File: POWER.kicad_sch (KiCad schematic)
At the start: 18 parts, among them IC1 ECP5-BGA256, U1 TPS74633, U2 TPS74618, U3 TPS74625, U4 TPS74611

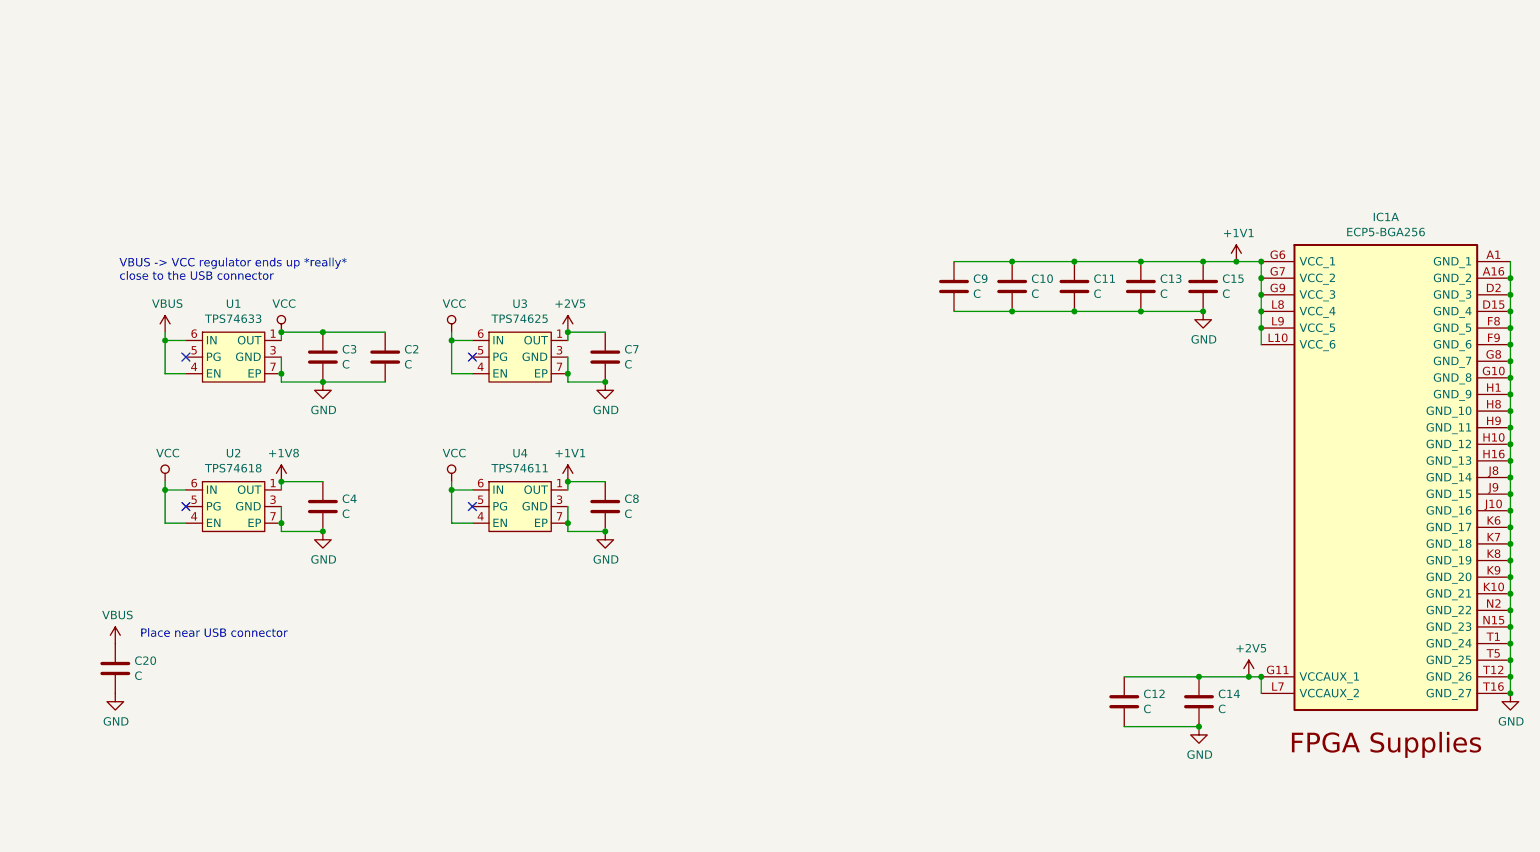
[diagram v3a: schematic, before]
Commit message: Change 1.8v and 3.3v regulators to buck for #2
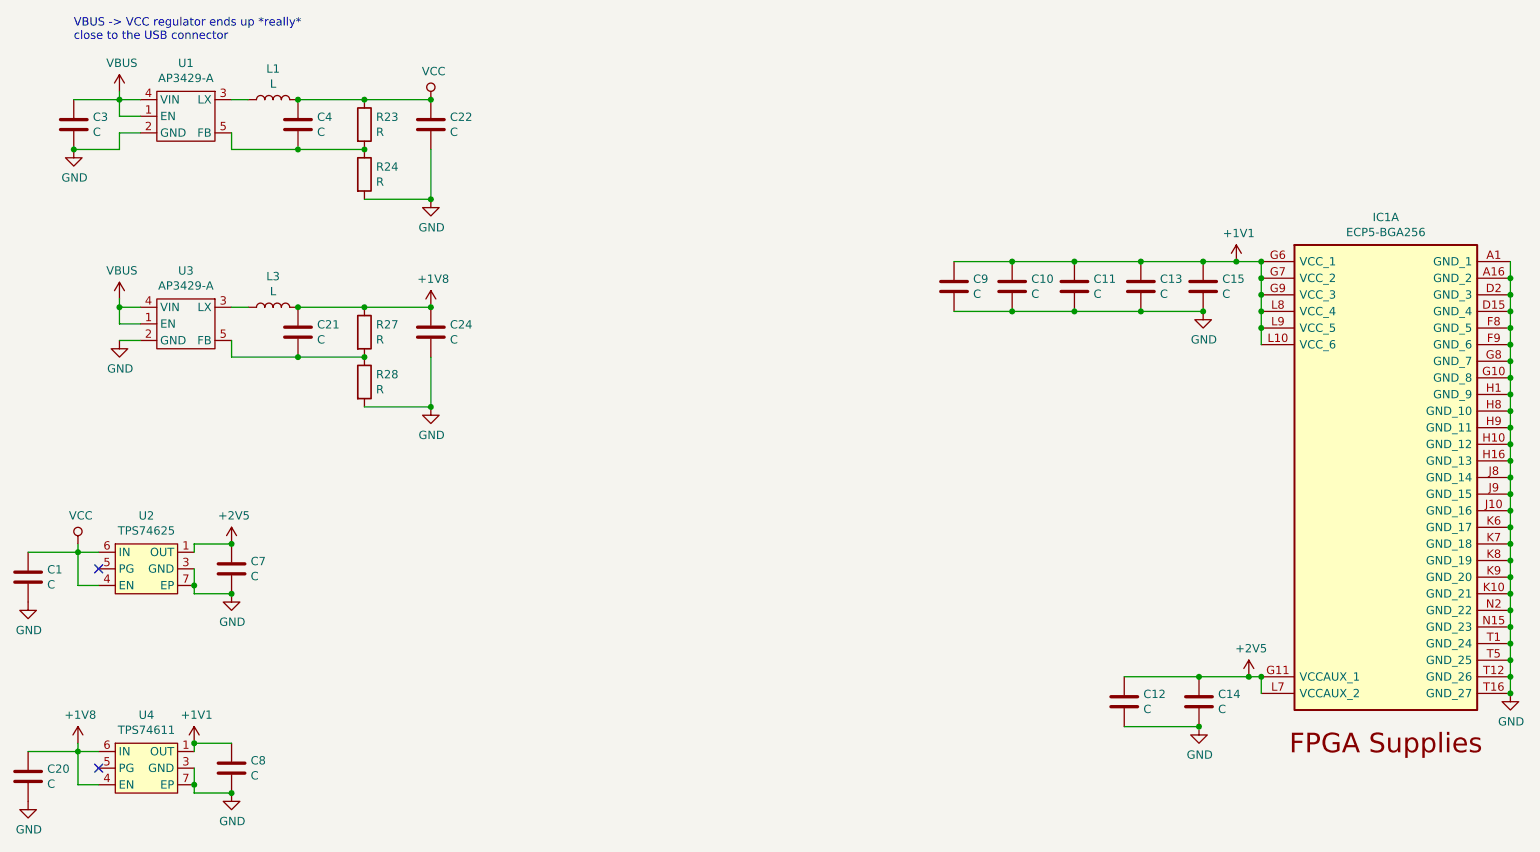
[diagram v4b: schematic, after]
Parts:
- removed C2: C, Capacitor_SMD:C_0805_2012Metric, symbol Device:C
- removed U1: TPS74633, Package_SON:WSON-6-1EP_2x2mm_P0.65mm_EP1x1.6mm, symbol mini_mipi:TPS74633
- removed U2: TPS74618, Package_SON:WSON-6-1EP_2x2mm_P0.65mm_EP1x1.6mm, symbol mini_mipi:TPS74618
- removed U3: TPS74625, Package_SON:WSON-6-1EP_2x2mm_P0.65mm_EP1x1.6mm, symbol mini_mipi:TPS74625
- added C1: C, Capacitor_SMD:C_0805_2012Metric, symbol Device:C
- added C21, C22, C24: C, Capacitor_SMD:C_0402_1005Metric, symbol Device:C
- added L1, L3: L, Inductor_SMD:L_1210_3225Metric, symbol Device:L
- added R23, R24, R27, R28: R, Resistor_SMD:R_0402_1005Metric, symbol Device:R
- added U1, U3: AP3429-A, Package_TO_SOT_SMD:TSOT-23-5, symbol mini_mipi:AP3429-A
- added U2: TPS74625, Package_SON:WSON-6-1EP_2x2mm_P0.65mm_EP1x1.6mm, symbol mini_mipi:TPS74625
- C4: footprint Capacitor_SMD:C_0805_2012Metric -> Capacitor_SMD:C_0402_1005Metric
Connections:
- net +1V8: now also C20.1, U4.4 (EN), U4.6 (IN), C21.1, C24.1, L3.2, R27.1; no longer C4.1
- net +2V5: now also U2.1 (OUT)
- net GND: now also C1.2, C22.2, C24.2, R24.2, R28.2, U1.2 (GND), U2.3 (GND), U2.7 (EP), U3.2 (GND); no longer C4.2
- net VBUS: now also C3.1, U1.1 (EN), U1.4 (VIN), U3.1 (EN), U3.4 (VIN); no longer C20.1
- net VCC: now also C4.1, C1.1, C22.1, L1.2, R23.1, U2.4 (EN), U2.6 (IN); no longer C3.1, U4.4 (EN), U4.6 (IN)
- new net: L3.1, U3.3 (LX)
- new net: C21.2, R27.2, R28.1, U3.5 (FB)
- new net: L1.1, U1.3 (LX)
- new net: C4.2, R23.2, R24.1, U1.5 (FB)
- no-connect marks 4 -> 2
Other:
- note removed: "Place near USB connector"
- moved on the sheet: C20, C3, C8, U4

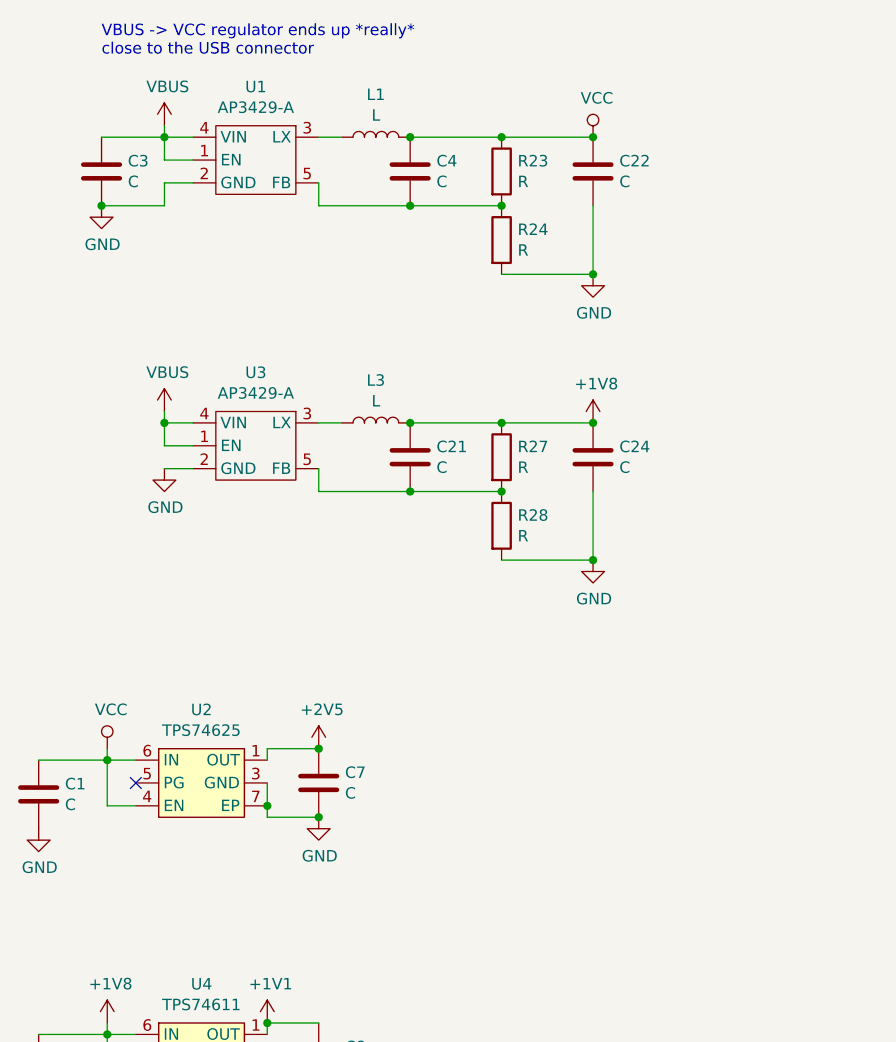
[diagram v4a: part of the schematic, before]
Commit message: Improve decoupling
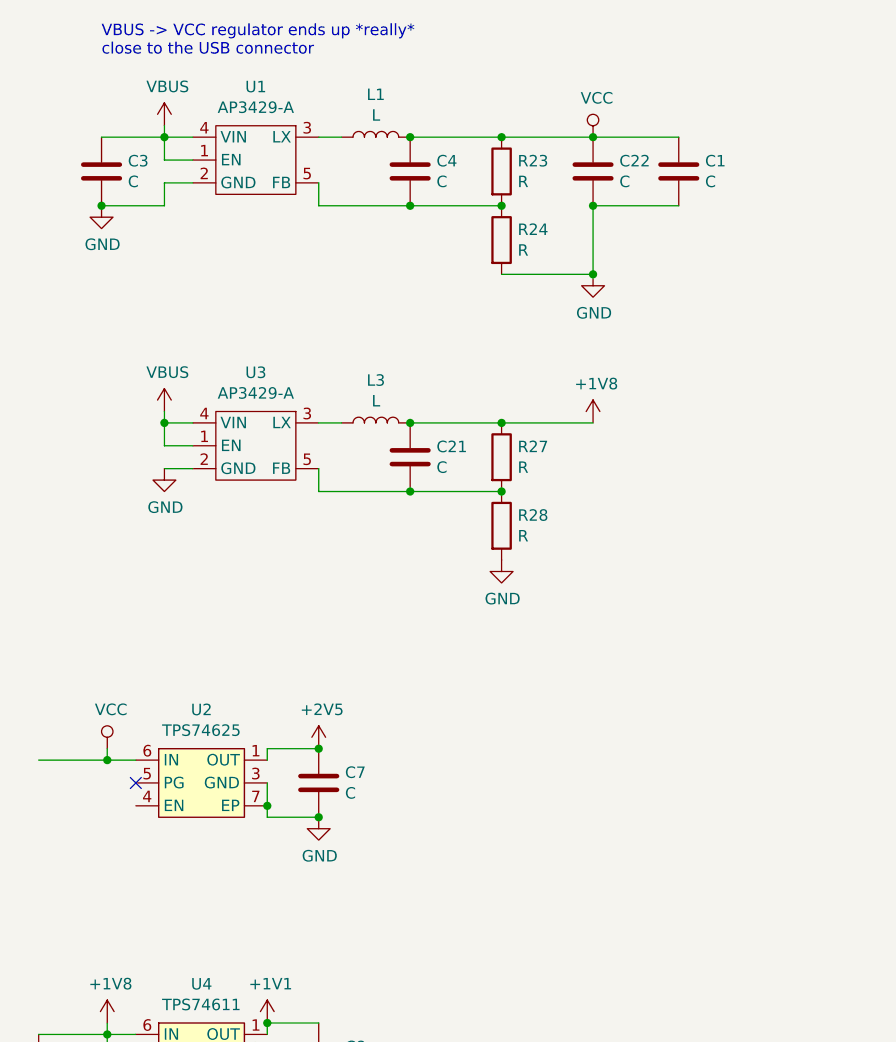
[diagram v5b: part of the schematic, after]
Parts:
- removed C24: C, Capacitor_SMD:C_0402_1005Metric, symbol Device:C
- C1: footprint Capacitor_SMD:C_0805_2012Metric -> Capacitor_SMD:C_0402_1005Metric
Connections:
- net VCC: no longer U2.4 (EN)
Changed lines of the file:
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@@
   (junction (at 73.025 75.565) (diameter 0) (color 0 0 0 0))
   (junction (at 83.185 36.195) (diameter 0) (color 0 0 0 0))
+  (junction (at 83.185 43.815) (diameter 0) (color 0 0 0 0))
   (junction (at 83.185 51.435) (diameter 0) (color 0 0 0 0))
-  (junction (at 83.185 67.945) (diameter 0) (color 0 0 0 0))
-  (junction (at 83.185 83.185) (diameter 0) (color 0 0 0 0))
   (junction (at 172.085 60.96) (diameter 0) (color 0 0 0 0))
   (junction (at 172.085 68.58) (diameter 0) (color 0 0 0 0))
@@
     (stroke (width 0) (type solid) (color 0 0 0 0))
   )
-  (wire (pts (xy 29.21 105.41) (xy 29.21 110.49))
-    (stroke (width 0) (type solid) (color 0 0 0 0))
-  )
   (wire (pts (xy 29.21 105.41) (xy 32.385 105.41))
     (stroke (width 0) (type solid) (color 0 0 0 0))
   )
-  (wire (pts (xy 29.21 110.49) (xy 32.385 110.49))
-    (stroke (width 0) (type solid) (color 0 0 0 0))
-  )
   (wire (pts (xy 29.21 134.62) (xy 29.21 135.89))
     (stroke (width 0) (type solid) (color 0 0 0 0))
@@
     (stroke (width 0) (type solid) (color 0 0 0 0))
   )
+  (wire (pts (xy 83.185 36.195) (xy 92.71 36.195))
+    (stroke (width 0) (type solid) (color 0 0 0 0))
+  )
   (wire (pts (xy 83.185 43.815) (xy 83.185 51.435))
     (stroke (width 0) (type solid) (color 0 0 0 0))
   )
+  (wire (pts (xy 83.185 43.815) (xy 92.71 43.815))
+    (stroke (width 0) (type solid) (color 0 0 0 0))
+  )
   (wire (pts (xy 83.185 51.435) (xy 73.025 51.435))
-    (stroke (width 0) (type solid) (color 0 0 0 0))
-  )
-  (wire (pts (xy 83.185 75.565) (xy 83.185 83.185))
-    (stroke (width 0) (type solid) (color 0 0 0 0))
-  )
-  (wire (pts (xy 83.185 83.185) (xy 73.025 83.185))
     (stroke (width 0) (type solid) (color 0 0 0 0))
   )
@@
     )
   )
-  (symbol (lib_id "power:GND") (at 21.59 113.03 0) (unit 1)
-    (in_bom yes) (on_board yes)
-    (property "Reference" "#PWR0151" (id 0) (at 21.59 119.38 0)
-      (effects (font (size 1.27 1.27)) hide)
-    )
-    (property "Value" "GND" (id 1) (at 21.7043 117.3544 0))
-    (property "Footprint" "" (id 2) (at 21.59 113.03 0)
-      (effects (font (size 1.27 1.27)) hide)
-    )
-    (property "Datasheet" "" (id 3) (at 21.59 113.03 0)
-      (effects (font (size 1.27 1.27)) hide)
-    )
-  )
   (symbol (lib_id "power:GND") (at 21.59 143.51 0) (unit 1)
     (in_bom yes) (on_board yes)
@@
     )
   )
+  (symbol (lib_id "power:GND") (at 73.025 83.185 0) (unit 1)
+    (in_bom yes) (on_board yes)
+    (property "Reference" "#PWR0109" (id 0) (at 73.025 89.535 0)
+      (effects (font (size 1.27 1.27)) hide)
+    )
+    (property "Value" "GND" (id 1) (at 73.1393 87.5094 0))
+    (property "Footprint" "" (id 2) (at 73.025 83.185 0)
+      (effects (font (size 1.27 1.27)) hide)
+    )
+    (property "Datasheet" "" (id 3) (at 73.025 83.185 0)
+      (effects (font (size 1.27 1.27)) hide)
+    )
+  )
   (symbol (lib_id "power:GND") (at 83.185 51.435 0) (unit 1)
     (in_bom yes) (on_board yes)
@@
     )
   )
-  (symbol (lib_id "power:GND") (at 83.185 83.185 0) (unit 1)
-    (in_bom yes) (on_board yes)
-    (property "Reference" "#PWR0109" (id 0) (at 83.185 89.535 0)
-      (effects (font (size 1.27 1.27)) hide)
-    )
-    (property "Value" "GND" (id 1) (at 83.2993 87.5094 0))
-    (property "Footprint" "" (id 2) (at 83.185 83.185 0)
-      (effects (font (size 1.27 1.27)) hide)
-    )
-    (property "Datasheet" "" (id 3) (at 83.185 83.185 0)
-      (effects (font (size 1.27 1.27)) hide)
-    )
-  )
   (symbol (lib_id "power:GND") (at 200.66 132.08 0) (unit 1)
     (in_bom yes) (on_board yes)
@@
     )
   )
-  (symbol (lib_id "Device:C") (at 21.59 109.22 0) (unit 1)
-    (in_bom yes) (on_board yes)
-    (property "Reference" "C1" (id 0) (at 24.5111 108.0706 0)
-      (effects (font (size 1.27 1.27)) (justify left))
-    )
-    (property "Value" "C" (id 1) (at 24.5111 110.3693 0)
-      (effects (font (size 1.27 1.27)) (justify left))
-    )
-    (property "Footprint" "Capacitor_SMD:C_0805_2012Metric" (id 2) (at 22.5552 113.03 0)
-      (effects (font (size 1.27 1.27)) hide)
-    )
-    (property "Datasheet" "~" (id 3) (at 21.59 109.22 0)
-      (effects (font (size 1.27 1.27)) hide)
-    )
-  )
   (symbol (lib_id "Device:C") (at 21.59 139.7 0) (unit 1)
     (in_bom yes) (on_board yes)
@@
     )
   )
-  (symbol (lib_id "Device:C") (at 83.185 71.755 0) (unit 1)
-    (in_bom yes) (on_board yes)
-    (property "Reference" "C24" (id 0) (at 86.1061 70.6056 0)
-      (effects (font (size 1.27 1.27)) (justify left))
-    )
-    (property "Value" "C" (id 1) (at 86.1061 72.9043 0)
-      (effects (font (size 1.27 1.27)) (justify left))
-    )
-    (property "Footprint" "Capacitor_SMD:C_0402_1005Metric" (id 2) (at 84.1502 75.565 0)
-      (effects (font (size 1.27 1.27)) hide)
-    )
-    (property "Datasheet" "~" (id 3) (at 83.185 71.755 0)
-      (effects (font (size 1.27 1.27)) hide)
-    )
+  (symbol (lib_id "Device:C") (at 92.71 40.005 0) (unit 1)
+    (in_bom yes) (on_board yes)
+    (property "Reference" "C1" (id 0) (at 95.6311 38.8556 0)
+      (effects (font (size 1.27 1.27)) (justify left))
+    )
+    (property "Value" "C" (id 1) (at 95.6311 41.1543 0)
+      (effects (font (size 1.27 1.27)) (justify left))
+    )
+    (property "Footprint" "Capacitor_SMD:C_0402_1005Metric" (id 2) (at 93.6752 43.815 0)
+      (effects (font (size 1.27 1.27)) hide)
+    )
+    (property "Datasheet" "~" (id 3) (at 92.71 40.005 0)
+      (effects (font (size 1.27 1.27)) hide)
+    )

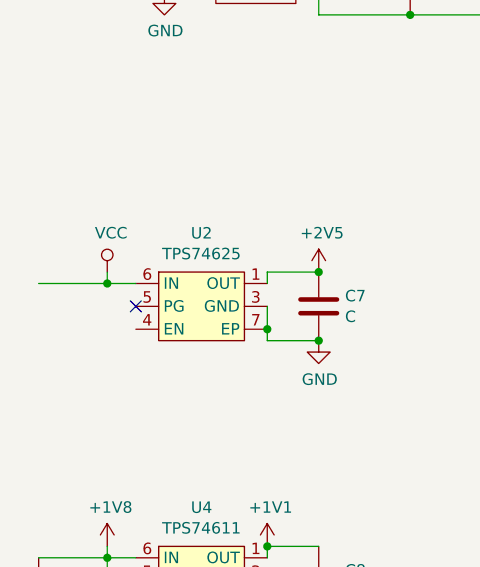
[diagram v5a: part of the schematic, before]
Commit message: Change debug header to 2.54mm standard
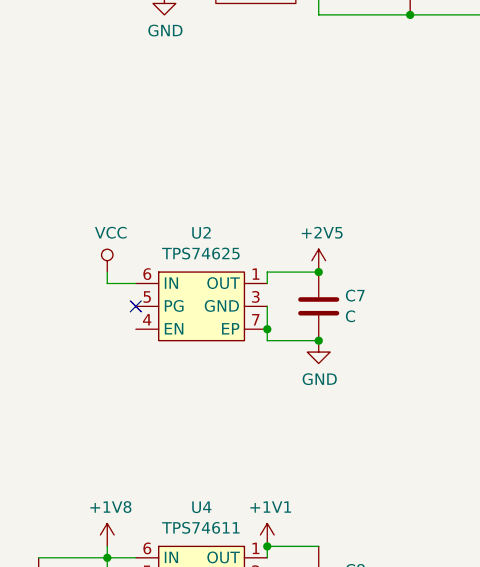
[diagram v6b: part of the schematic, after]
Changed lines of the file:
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@@
-(kicad_sch (version 20200714) (host eeschema "5.99.0-unknown-a61ea1f~102~ubuntu20.04.1")
-  (page 5 6)
+(kicad_sch (version 20200714) (host eeschema "5.99.0-unknown-8324cb3~102~ubuntu20.04.1")
+  (page 1 6)
   (paper "A4")
   (junction (at 28.575 43.815) (diameter 0) (color 0 0 0 0))
-  (junction (at 29.21 105.41) (diameter 0) (color 0 0 0 0))
   (junction (at 29.21 135.89) (diameter 0) (color 0 0 0 0))
   (junction (at 35.56 36.195) (diameter 0) (color 0 0 0 0))
@@
   (junction (at 248.285 124.46) (diameter 0) (color 0 0 0 0))
   (junction (at 248.285 127) (diameter 0) (color 0 0 0 0))
+  (no_connect (at 32.385 107.95))
   (no_connect (at 32.385 138.43))
-  (no_connect (at 32.385 107.95))
-  (wire (pts (xy 21.59 105.41) (xy 29.21 105.41))
-    (stroke (width 0) (type solid) (color 0 0 0 0))
-  )
   (wire (pts (xy 21.59 135.89) (xy 29.21 135.89))
     (stroke (width 0) (type solid) (color 0 0 0 0))
